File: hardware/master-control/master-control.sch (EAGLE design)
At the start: 47 parts, among them IC101 LM22672, IC102 TLV70033_DDC, IC201 ATxmega128A3-AU, X101 87832-06, X2 22-23-2071, X201 87832-10, Y200 ABM8G

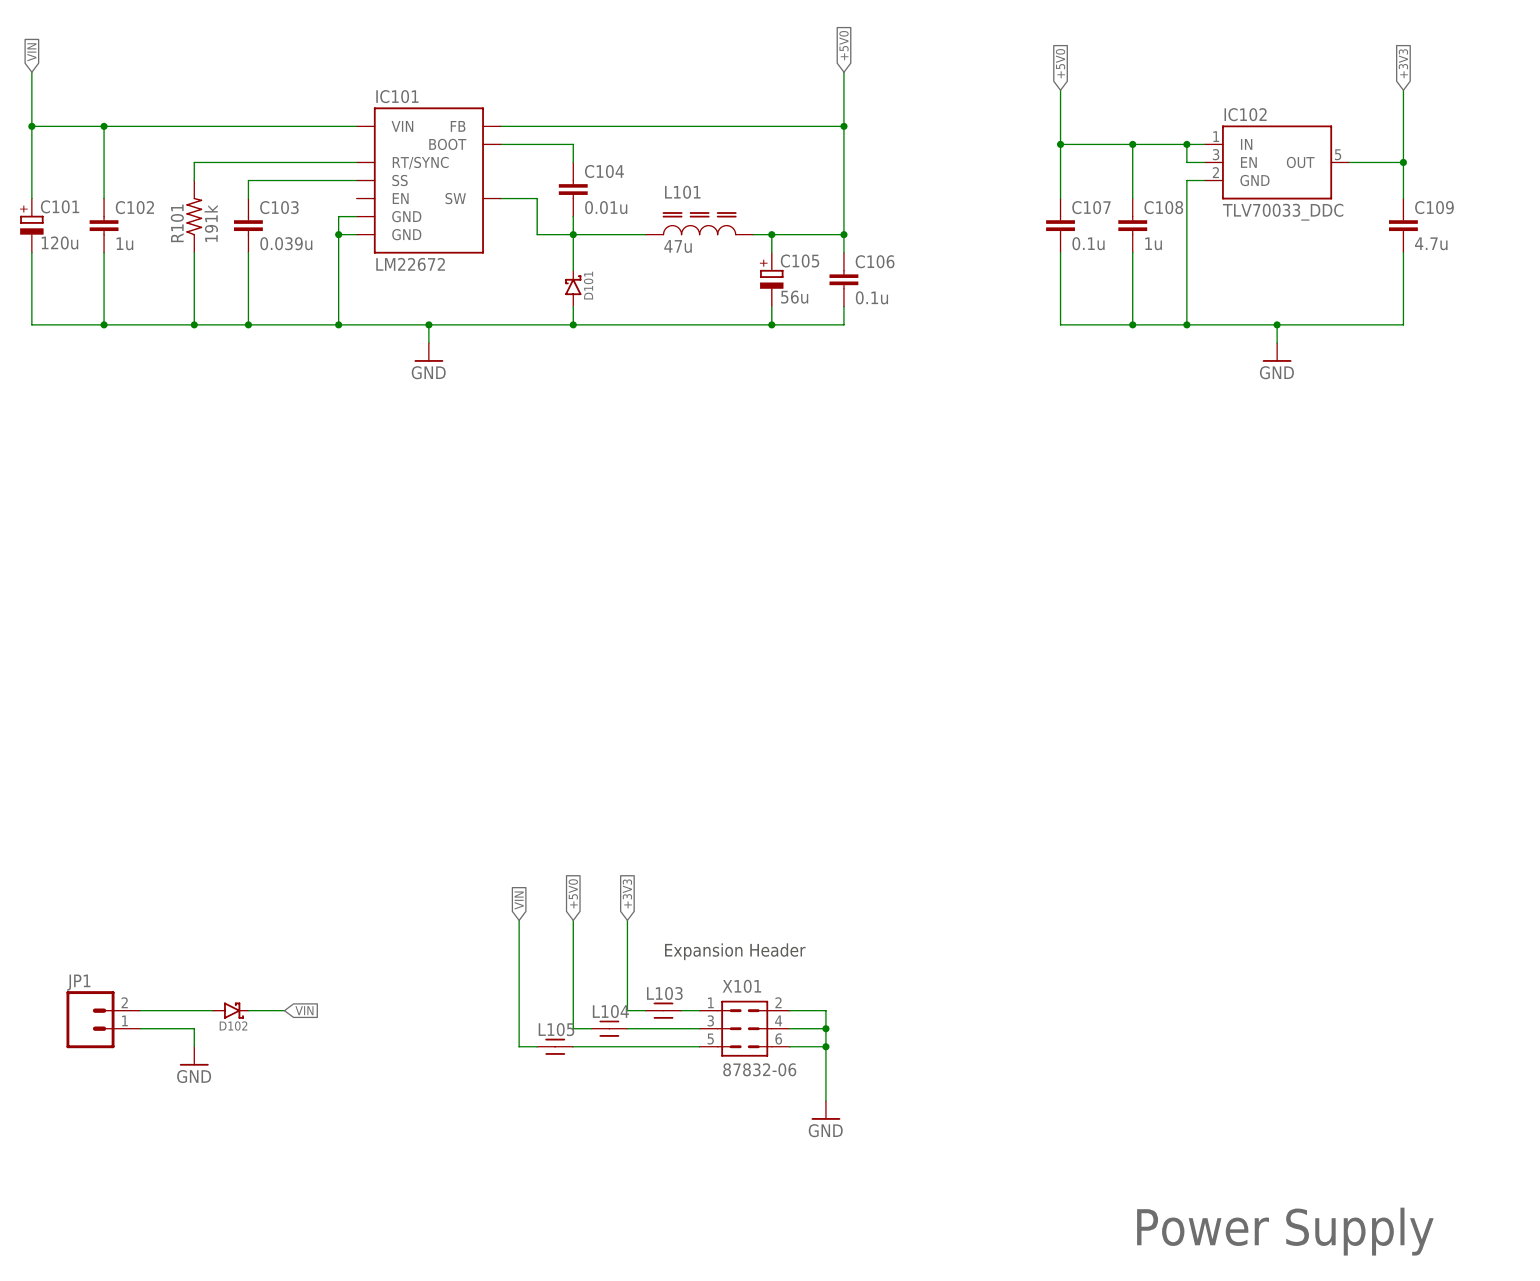
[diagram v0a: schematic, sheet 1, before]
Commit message: Add data sheets folder. Make changes to master-control to eliminate LCD and keypad, begin adding isoSPI ICs.
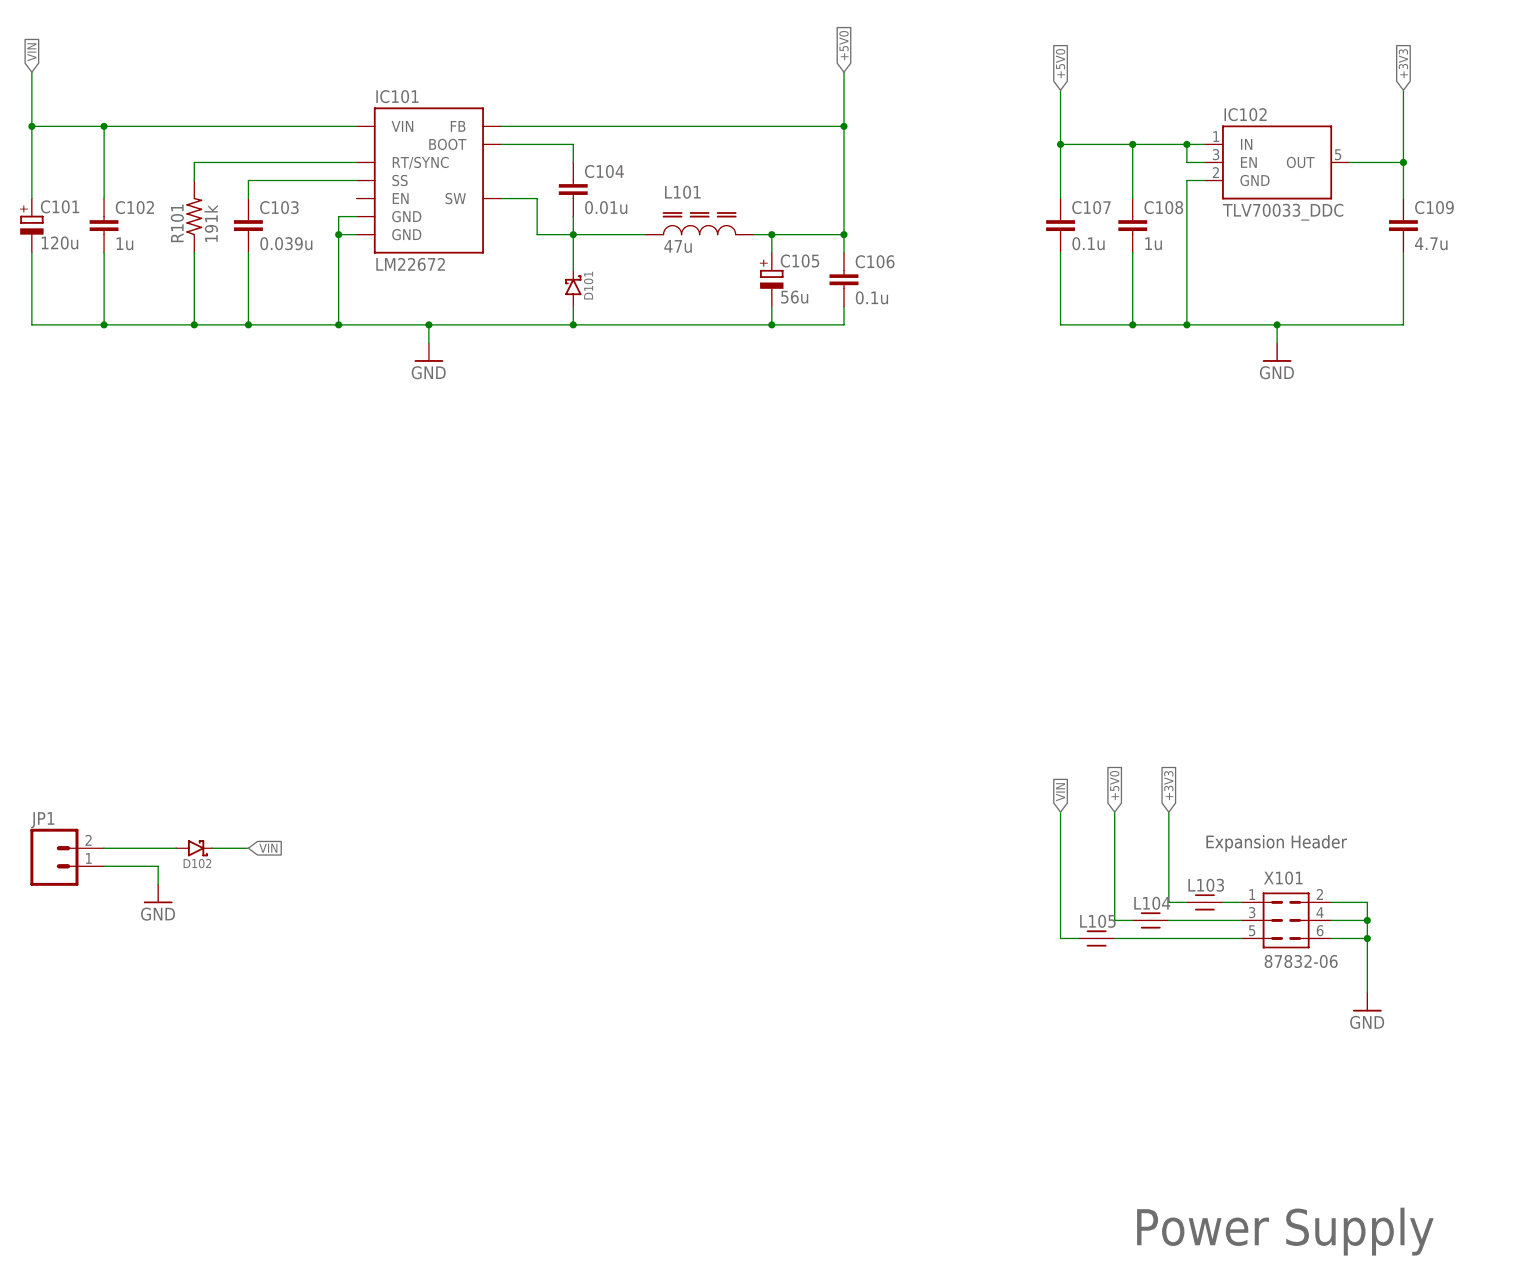
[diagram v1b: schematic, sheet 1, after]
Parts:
- removed C210: 1u, rcl:C-EUC0603
- removed C211: 0.1u, rcl:C-EUC0603
- removed LCD1: LS027, m_opto:SHARP_LS0-FPC-MEMORY-LCD
- removed X2: 22-23-2071, con-molex:22-23-2071
- added IC1: (no value), m_ic-comm:LTC6820_MS
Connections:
- removed net LCD_DISP: IC201.PE0, LCD1.DISP
- removed net LCD_SCLK: IC201.PE1, LCD1.SCLK
- removed net LCD_SCS: IC201.PE2, LCD1.SCS
- removed net LCD_SI: IC201.PE3, LCD1.SI
- removed net N$10: IC201.PC4, X2-3.S
- removed net N$11: IC201.PC3, X2-4.S
- removed net N$12: IC201.PC2, X2-5.S
- removed net N$13: IC201.PC1, X2-6.S
- removed net N$14: IC201.PC0, X2-7.S
- removed net N$15: IC201.PC6, X2-1.S
- removed net N$9: IC201.PC5, X2-2.S
- net !SD_CS: now also IC201.PE0; no longer IC201.PE4
- net +5V0: no longer C210.1, C211.1, LCD1.VDD, LCD1.VDDA
- net GND: no longer C210.2, C211.2, LCD1.EXTCOMIN, LCD1.EXTMODE, LCD1.VSS, LCD1.VSSA
- net SD_MISO: now also IC201.PE2; no longer IC201.PE6
- net SD_MOSI: now also IC201.PE3; no longer IC201.PE7
- net SD_SCK: now also IC201.PE1; no longer IC201.PE5
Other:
- note removed: "Keypad"
- note removed: "LCD Interface"
- moved on the sheet: D102, JP1, L103, L104, L105, X101
